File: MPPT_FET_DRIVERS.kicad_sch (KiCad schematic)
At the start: 18 parts, among them U13 XJNG2103, U17 XJNG2103

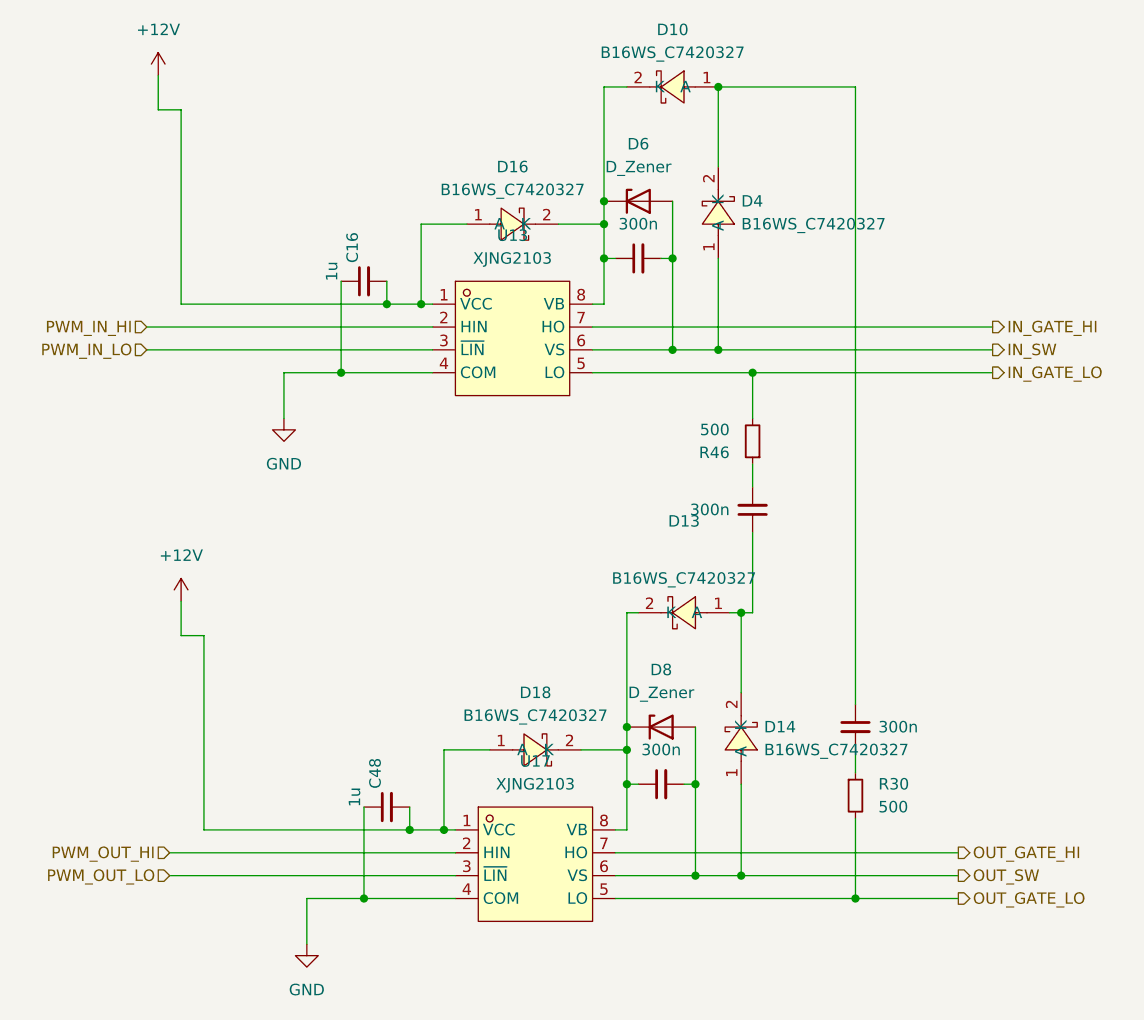
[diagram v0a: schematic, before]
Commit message: latest version with PWM fan and thermistors for each FET bank
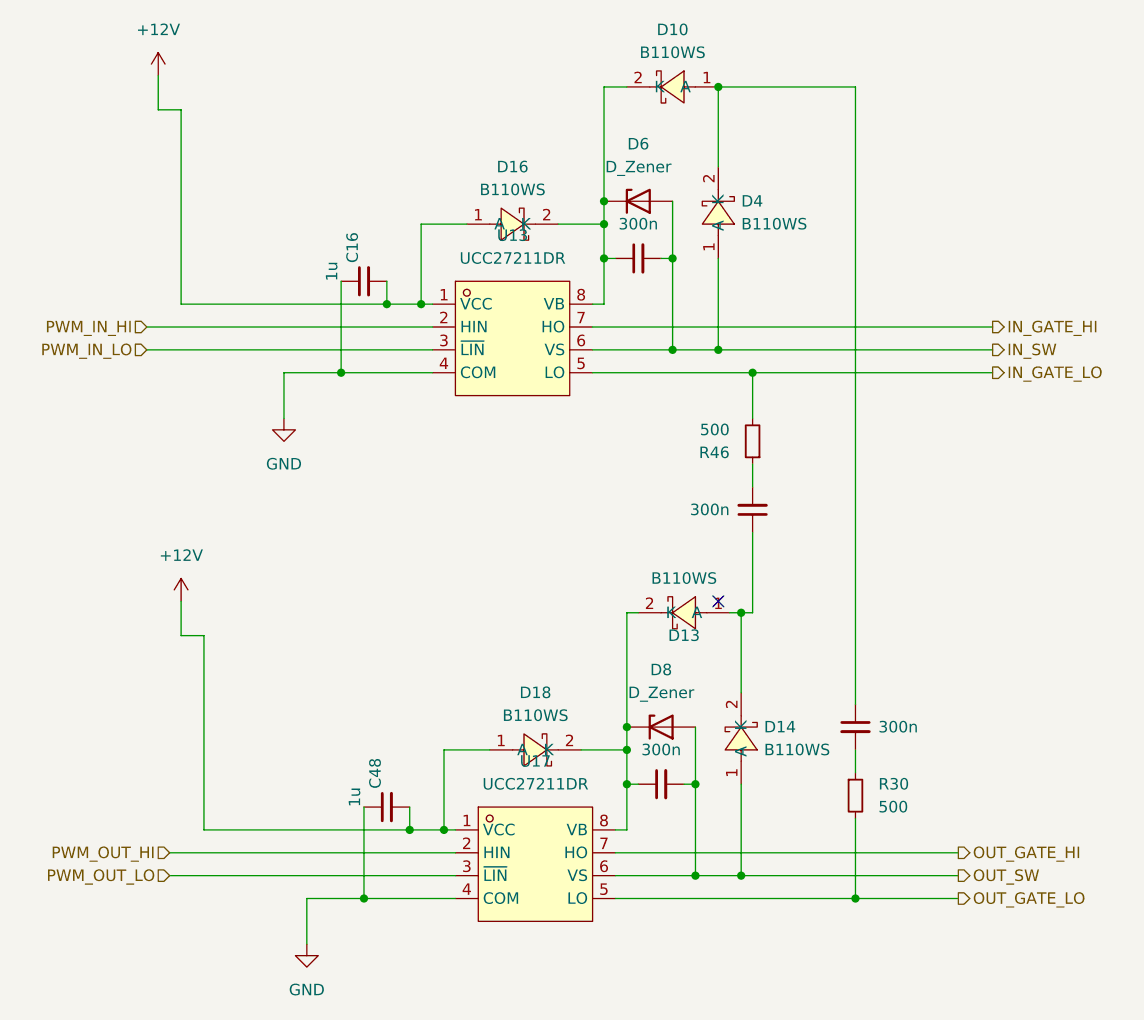
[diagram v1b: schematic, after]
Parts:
- C14, C18, C65, C8: LCSC Part (none) -> C609906
- C16, C48: LCSC Part (none) -> C466612
- D10, D13, D14, D16, D18, D4: value B16WS_C7420327 -> B110WS; LCSC Part C7420327 -> C7461125
- D6, D8: LCSC Part (none) -> C20611962
- R30, R46: LCSC Part (none) -> C25905
- U13, U17: value XJNG2103 -> UCC27211DR; LCSC Part C2887735 -> C2871979
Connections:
- no-connect marks 0 -> 1
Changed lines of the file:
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@@
 		(color 0 0 0 0)
+	)
+	(no_connect
+		(at 176.53 102.87)
 	)
 	(wire
@@
 			)
 		)
-		(property "Value" "B16WS_C7420327"
+		(property "Value" "B110WS"
 			(at 181.61 119.3799 90)
 			(effects
@@
 			)
 		)
-		(property "LCSC Part" "C7420327"
+		(property "LCSC Part" "C7461125"
 			(at 189.23 118.11 0)
 			(effects
@@
 			)
 		)
+		(property "LCSC Part" "C20611962"
+			(at 167.64 58.42 0)
+			(effects
+				(font
+					(size 1.27 1.27)
+				)
+				(hide yes)
+			)
+		)
 		(pin "1"
 		)
@@
 		(property "Description" "Unpolarized capacitor, small symbol"
 			(at 180.34 92.71 0)
+			(effects
+				(font
+					(size 1.27 1.27)
+				)
+				(hide yes)
+			)
+		)
+		(property "LCSC Part" "C609906"
+			(at 180.34 92.71 90)
 			(effects
 				(font
@@
 			)
 		)
+		(property "LCSC Part" "C466612"
+			(at 137.16 67.31 0)
+			(effects
+				(font
+					(size 1.27 1.27)
+				)
+				(hide yes)
+			)
+		)
 		(pin "2"
 		)
@@
 			)
 		)
-		(property "Value" "B16WS_C7420327"
+		(property "Value" "B110WS"
 			(at 171.45 41.91 0)
 			(effects
@@
 			)
 		)
-		(property "LCSC Part" "C7420327"
+		(property "LCSC Part" "C7461125"
 			(at 171.45 35.56 0)
 			(effects
@@
 			)
 		)
-		(property "Value" "XJNG2103"
+		(property "Value" "UCC27211DR"
 			(at 156.21 123.19 0)
 			(effects
@@
 			)
 		)
-		(property "LCSC Part" "C2887735"
+		(property "LCSC Part" "C2871979"
 			(at 156.21 146.05 0)
 			(effects
@@
 			)
 		)
+		(property "LCSC Part" "C25905"
+			(at 191.77 124.46 0)
+			(effects
+				(font
+					(size 1.27 1.27)
+				)
+				(hide yes)
+			)
+		)
 		(pin "1"
 		)
@@
 			)
 		)
-		(property "Value" "B16WS_C7420327"
+		(property "Value" "B110WS"
 			(at 156.21 115.57 0)
 			(effects
@@
 			)
 		)
-		(property "LCSC Part" "C7420327"
+		(property "LCSC Part" "C7461125"
 			(at 156.21 129.54 0)
 			(effects
@@
 			)
 		)
+		(property "LCSC Part" "C609906"
+			(at 167.64 64.77 90)
+			(effects
+				(font
+					(size 1.27 1.27)
+				)
+				(hide yes)
+			)
+		)
 		(pin "2"
 		)
@@
 			)
 		)
-		(property "Value" "XJNG2103"
+		(property "Value" "UCC27211DR"
 			(at 153.67 64.77 0)
 			(effects
@@
 			)
 		)
-		(property "LCSC Part" "C2887735"
+		(property "LCSC Part" "C2871979"
 			(at 153.67 87.63 0)
 			(effects
@@
 			)
 		)
-		(property "Value" "B16WS_C7420327"
+		(property "Value" "B110WS"
 			(at 153.67 57.15 0)
 			(effects
@@
 			)
 		)
-		(property "LCSC Part" "C7420327"
+		(property "LCSC Part" "C7461125"
 			(at 153.67 71.12 0)
 			(effects
@@
 		)
 		(property "Description" "Zener diode"
+			(at 170.18 116.84 0)
+			(effects
+				(font
+					(size 1.27 1.27)
+				)
+				(hide yes)
+			)
+		)
+		(property "LCSC Part" "C20611962"
 			(at 170.18 116.84 0)
 			(effects
@@
 		(dnp no)
 		(property "Reference" "D13"
-			(at 172.72 93.98 0)
-			(effects
-				(font
-					(size 1.27 1.27)
-				)
-			)
-		)
-		(property "Value" "B16WS_C7420327"
+			(at 172.72 106.68 0)
+			(effects
+				(font
+					(size 1.27 1.27)
+				)
+			)
+		)
+		(property "Value" "B110WS"
 			(at 172.72 100.33 0)
 			(effects
@@
 			)
 		)
-		(property "LCSC Part" "C7420327"
+		(property "LCSC Part" "C7461125"
 			(at 172.72 93.98 0)
 			(effects
@@
 			)
 		)
-		(property "Value" "B16WS_C7420327"
+		(property "Value" "B110WS"
 			(at 179.07 60.9599 90)
 			(effects
@@
 			)
 		)
-		(property "LCSC Part" "C7420327"
+		(property "LCSC Part" "C7461125"
 			(at 186.69 59.69 0)
 			(effects
@@
 			)
 		)
+		(property "LCSC Part" "C25905"
+			(at 180.34 85.09 0)
+			(effects
+				(font
+					(size 1.27 1.27)
+				)
+				(hide yes)
+			)
+		)
 		(pin "1"
 		)
@@
 		(property "Description" "Unpolarized capacitor, small symbol"
 			(at 170.18 123.19 0)
+			(effects
+				(font
+					(size 1.27 1.27)
+				)
+				(hide yes)
+			)
+		)
+		(property "LCSC Part" "C609906"
+			(at 170.18 123.19 90)
 			(effects
 				(font
@@
 			)
 		)
+		(property "LCSC Part" "C466612"
+			(at 139.7 125.73 0)
+			(effects
+				(font
+					(size 1.27 1.27)
+				)
+				(hide yes)
+			)
+		)
 		(pin "2"
 		)
@@
 			(effects
 				(font
+					(size 1.27 1.27)
+				)
+				(hide yes)
+			)
+		)
+		(property "LCSC Part" "C609906"
+			(at 191.77 116.84 90)
+			(effects
+				(font

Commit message: production version v3
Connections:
- no-connect marks 1 -> 0
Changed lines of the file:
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@@
 		(color 0 0 0 0)
-	)
-	(no_connect
-		(at 176.53 102.87)
 	)
 	(wire
